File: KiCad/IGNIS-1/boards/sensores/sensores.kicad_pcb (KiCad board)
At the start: 2 copper layers, 62 x 62 mm, 16 parts, among them J41 Backplane_2x10, U20 BME280, U21 MPU6050, U22 MQ-135, U24 GPS NEO-6M, U3 Boost_5V

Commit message: Update antes de mover a 4o board
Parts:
- C20: footprint Capacitor_SMD:C_0805_2012Metric -> Capacitor_THT:C_Disc_D7.5mm_W2.5mm_P5.00mm
- C4: footprint Capacitor_SMD:C_1210_3225Metric -> Capacitor_THT:CP_Radial_D13.0mm_P5.00mm
- J41: footprint Connector_PinHeader_2.54mm:PinHeader_2x10_P2.54mm_Vertical -> Connector_IDC:IDC-Header_2x10_P2.54mm_Vertical
- R20, R21, R22, R23: footprint Resistor_SMD:R_0805_2012Metric -> Resistor_THT:R_Axial_DIN0207_L6.3mm_D2.5mm_P7.62mm_Horizontal
- U21: footprint Connector_PinHeader_2.54mm:PinHeader_1x08_P2.54mm_Vertical -> IGNIS1:MPU6050_module
- U3: footprint Connector_PinHeader_2.54mm:PinHeader_1x04_P2.54mm_Vertical -> IGNIS1:MT3608_module
- moved U3 25.8 mm to (49.4, 104.1)
- moved U21 14.5 mm to (133.9, 93.3)
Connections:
- net /MQ_A0_RAW renamed Net-(U22-A0)
- U3 pad 3: +3V3 -> +5V
- U3 pad 4: +5V -> GND
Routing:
- net Net-(U22-A0): track 16.6 -> 0.00 mm
- net (no net): track 0.00 -> 16.6 mm

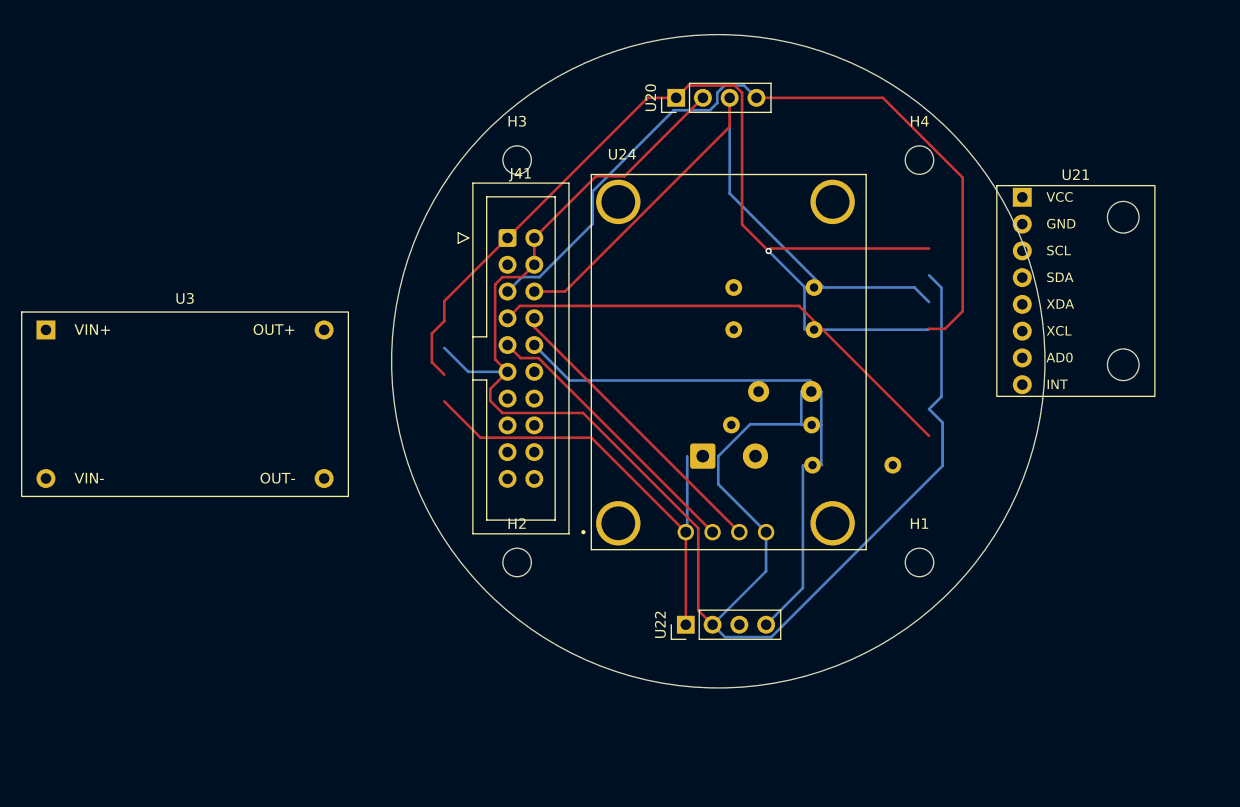
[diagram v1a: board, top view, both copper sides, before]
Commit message: Updated board de sensores
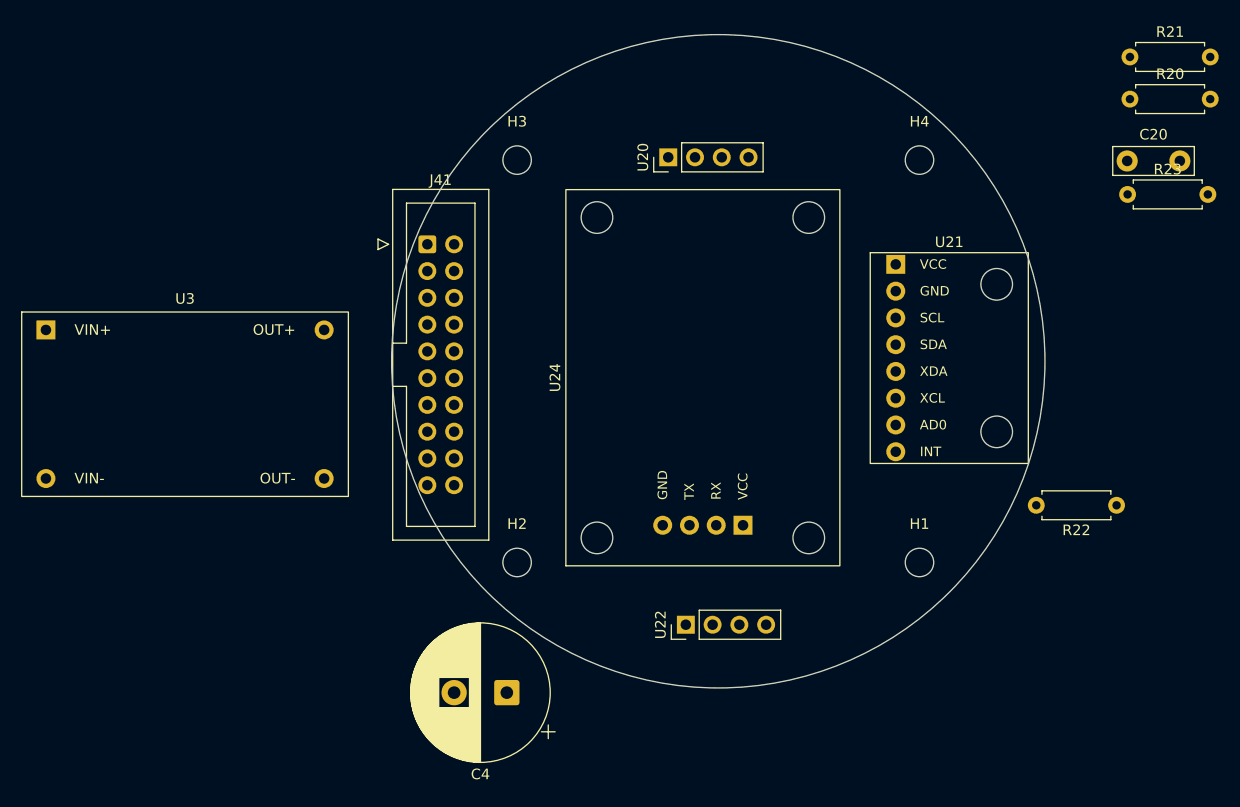
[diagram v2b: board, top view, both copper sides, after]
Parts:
- C20, C4, R20, R21, R22, R23: moved to F.Cu
- U24: footprint ZC323200:XCVR_ZC323200 -> IGNIS1:GPS_NEO6M_module
- moved C20 37.1 mm to (138.8, 81.0), turned to 0 degrees
- moved R23 37.1 mm to (138.8, 84.2), turned to 0 degrees
- moved R20 37.1 mm to (139.1, 75.1), turned to 0 degrees
- moved R21 37.1 mm to (139.1, 71.1), turned to 0 degrees
- moved C4 29.1 mm to (79.9, 131.4), turned to 180 degrees
- moved R22 29.1 mm to (137.8, 113.7), turned to 180 degrees
- moved U21 13.6 mm to (121.9, 99.7)
- moved J41 7.63 mm to (72.4, 88.9)
- moved U20 5.69 mm to (95.2, 80.6)
- moved U24 2.96 mm to (98.5, 101.6), turned to 90 degrees
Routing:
- net GND: track 163.1 -> 0.00 mm
- net +3V3: track 85.2 -> 0.00 mm, vias 1 -> 0
- net SDA: track 83.9 -> 0.00 mm
- net SCL: track 60.0 -> 0.00 mm
- net MPU_INT: track 45.6 -> 0.00 mm
- net +5V: track 44.1 -> 0.00 mm
- net MQ_AOUT: track 36.1 -> 0.00 mm
- net GPS_TX: track 28.4 -> 0.00 mm
- net GPS_RX: track 26.8 -> 0.00 mm
- net (no net): track 16.6 -> 0.00 mm
